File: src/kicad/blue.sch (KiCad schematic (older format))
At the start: 0 parts

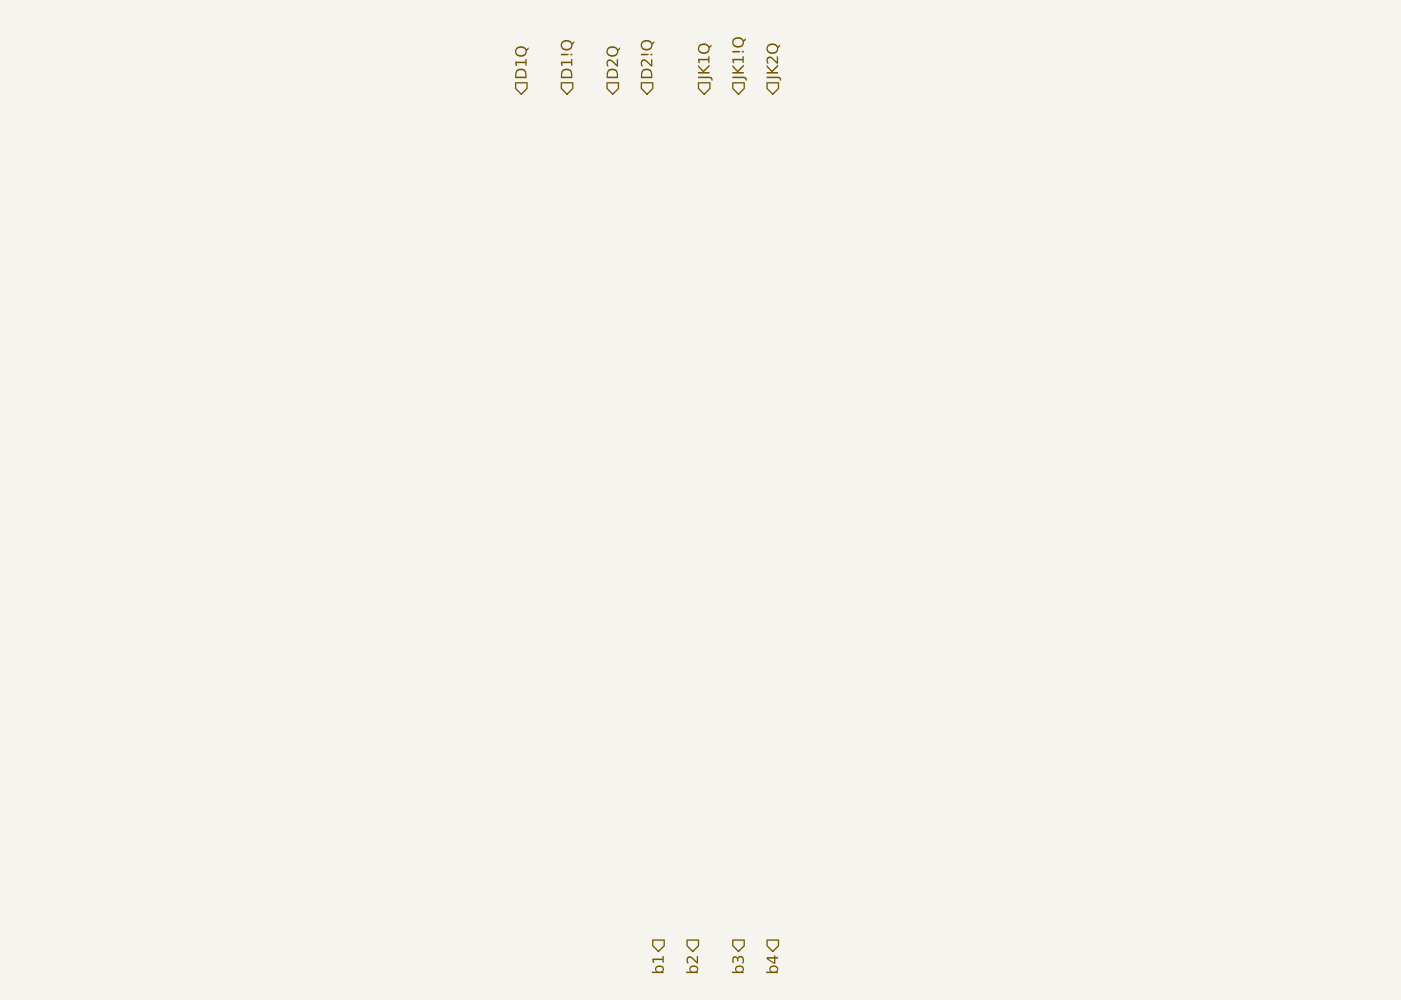
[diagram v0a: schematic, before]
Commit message: finished sub-schemes for LEDs
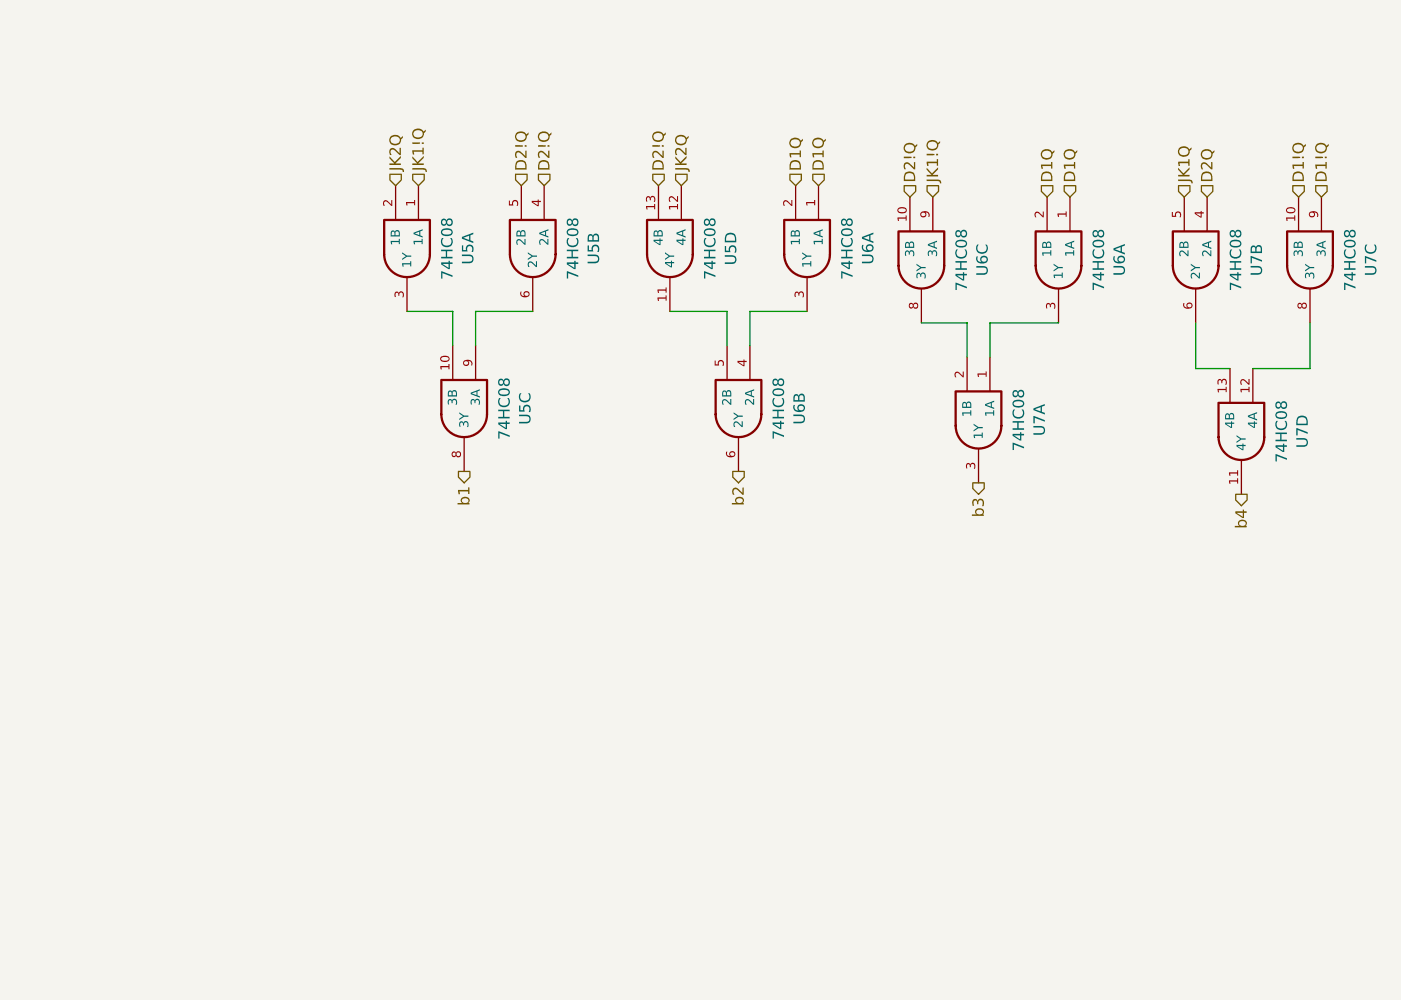
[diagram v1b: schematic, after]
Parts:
- added U5, U6 (x2), U7: 74HC08, Housings_SOIC:SOIC-14_3.9x8.7mm_Pitch1.27mm, symbol PB170:74HC08
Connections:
- net D1!Q: now also U7.10 (3B), U7.9 (3A)
- net D1Q: now also U6.1 (1A), U6.1 (1A), U6.2 (1B), U6.2 (1B)
- net D2!Q: now also U5.13 (4B), U5.4 (2A), U5.5 (2B), U6.10 (3B)
- net D2Q: now also U7.4 (2A)
- net JK1!Q: now also U5.1 (1A), U6.9 (3A)
- net JK1Q: now also U7.5 (2B)
- net JK2Q: now also U5.12 (4A), U5.2 (1B)
- net b1: now also U5.8 (3Y)
- net b2: now also U6.6 (2Y)
- net b3: now also U7.3 (1Y)
- net b4: now also U7.11 (4Y)
- new net: U5.10 (3B), U5.3 (1Y)
- new net: U5.6 (2Y), U5.9 (3A)
- new net: U5.11 (4Y), U6.5 (2B)
- new net: U6.3 (1Y), U6.4 (2A)
- new net: U6.8 (3Y), U7.2 (1B)
- new net: U6.3 (1Y), U7.1 (1A)
- new net: U7.13 (4B), U7.6 (2Y)
- new net: U7.12 (4A), U7.8 (3Y)

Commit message: fixed annotaion
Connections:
- net D1Q: now also U6.12 (4A), U6.13 (4B); no longer U6.1 (1A), U6.2 (1B)
- net at U7.1 (1A): now also U6.11 (4Y); no longer U6.3 (1Y)
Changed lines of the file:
@@
 $Descr A4 11693 8268
 encoding utf-8
-Sheet 4 6
+Sheet 3 5
 Title ""
 Date ""
@@
 $Comp
 L PB170:74HC08 U?
-U 1 1 5FFF44C7
+U 4 1 5FFF44C7
 P 5150 2700
 AR Path="/5FFF44C7" Ref="U?"  Part="2"
 AR Path="/6006FC3B/5FFF44C7" Ref="U?"  Part="4"
-AR Path="/6004480C/5FFF44C7" Ref="U6"  Part="1"
+AR Path="/6004480C/5FFF44C7" Ref="U6"  Part="4"
 F 0 "U6" H 5175 2967 50  0000 C CNN
 F 1 "74HC08" H 5175 2876 50  0000 C CNN
@@
 F 3 "https://datasheet.lcsc.com/szlcsc/Nexperia-74HC08D-653_C5593.pdf" H 5150 2700 50  0001 C CNN
 F 4 "C5593" H 5150 2700 50  0001 C CNN "LCSC"
-	1    5150 2700
+	4    5150 2700
 	0    1    1    0
 $EndComp

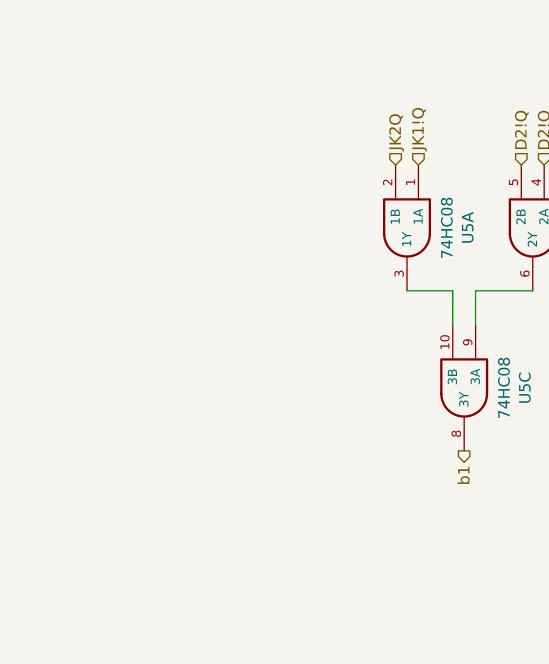
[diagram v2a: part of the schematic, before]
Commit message: added annotations, power connections to parts
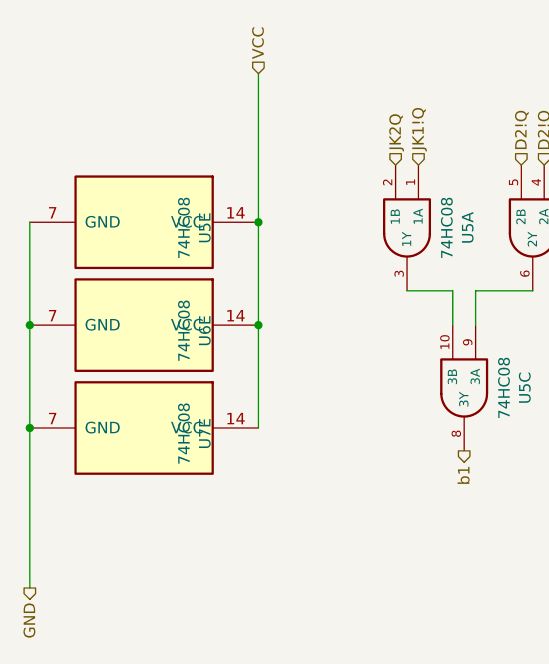
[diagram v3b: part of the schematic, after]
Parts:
- added unit 5 of U5
- added unit 5 of U6
- added unit 5 of U7
- U5, U6, U7: footprint Housings_SOIC:SOIC-14_3.9x8.7mm_Pitch1.27mm -> Package_SO:SOIC-14_3.9x8.7mm_P1.27mm
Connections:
- new net GND: U5.7 (GND), U6.7 (GND), U7.7 (GND)
- new net VCC: U5.14 (VCC), U6.14 (VCC), U7.14 (VCC)
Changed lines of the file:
@@
 F 0 "U5" H 2325 2917 50  0000 C CNN
 F 1 "74HC08" H 2325 2826 50  0000 C CNN
-F 2 "Housings_SOIC:SOIC-14_3.9x8.7mm_Pitch1.27mm" H 2300 2650 50  0001 C CNN
+F 2 "Package_SO:SOIC-14_3.9x8.7mm_P1.27mm" H 2300 2650 50  0001 C CNN
 F 3 "https://datasheet.lcsc.com/szlcsc/Nexperia-74HC08D-653_C5593.pdf" H 2300 2650 50  0001 C CNN
 F 4 "C5593" H 2300 2650 50  0001 C CNN "LCSC"
@@
 F 0 "U5" H 2875 2917 50  0000 C CNN
 F 1 "74HC08" H 2875 2826 50  0000 C CNN
-F 2 "Housings_SOIC:SOIC-14_3.9x8.7mm_Pitch1.27mm" H 2850 2650 50  0001 C CNN
+F 2 "Package_SO:SOIC-14_3.9x8.7mm_P1.27mm" H 2850 2650 50  0001 C CNN
 F 3 "https://datasheet.lcsc.com/szlcsc/Nexperia-74HC08D-653_C5593.pdf" H 2850 2650 50  0001 C CNN
 F 4 "C5593" H 2850 2650 50  0001 C CNN "LCSC"
@@
 F 0 "U5" H 2575 3617 50  0000 C CNN
 F 1 "74HC08" H 2575 3526 50  0000 C CNN
-F 2 "Housings_SOIC:SOIC-14_3.9x8.7mm_Pitch1.27mm" H 2550 3350 50  0001 C CNN
+F 2 "Package_SO:SOIC-14_3.9x8.7mm_P1.27mm" H 2550 3350 50  0001 C CNN
 F 3 "https://datasheet.lcsc.com/szlcsc/Nexperia-74HC08D-653_C5593.pdf" H 2550 3350 50  0001 C CNN
 F 4 "C5593" H 2550 3350 50  0001 C CNN "LCSC"
@@
 F 0 "U5" H 3475 2917 50  0000 C CNN
 F 1 "74HC08" H 3475 2826 50  0000 C CNN
-F 2 "Housings_SOIC:SOIC-14_3.9x8.7mm_Pitch1.27mm" H 3450 2650 50  0001 C CNN
+F 2 "Package_SO:SOIC-14_3.9x8.7mm_P1.27mm" H 3450 2650 50  0001 C CNN
 F 3 "https://datasheet.lcsc.com/szlcsc/Nexperia-74HC08D-653_C5593.pdf" H 3450 2650 50  0001 C CNN
 F 4 "C5593" H 3450 2650 50  0001 C CNN "LCSC"
@@
 F 0 "U6" H 4075 2917 50  0000 C CNN
 F 1 "74HC08" H 4075 2826 50  0000 C CNN
-F 2 "Housings_SOIC:SOIC-14_3.9x8.7mm_Pitch1.27mm" H 4050 2650 50  0001 C CNN
+F 2 "Package_SO:SOIC-14_3.9x8.7mm_P1.27mm" H 4050 2650 50  0001 C CNN
 F 3 "https://datasheet.lcsc.com/szlcsc/Nexperia-74HC08D-653_C5593.pdf" H 4050 2650 50  0001 C CNN
 F 4 "C5593" H 4050 2650 50  0001 C CNN "LCSC"
@@
 F 0 "U6" H 3775 3617 50  0000 C CNN
 F 1 "74HC08" H 3775 3526 50  0000 C CNN
-F 2 "Housings_SOIC:SOIC-14_3.9x8.7mm_Pitch1.27mm" H 3750 3350 50  0001 C CNN
+F 2 "Package_SO:SOIC-14_3.9x8.7mm_P1.27mm" H 3750 3350 50  0001 C CNN
 F 3 "https://datasheet.lcsc.com/szlcsc/Nexperia-74HC08D-653_C5593.pdf" H 3750 3350 50  0001 C CNN
 F 4 "C5593" H 3750 3350 50  0001 C CNN "LCSC"
@@
 F 0 "U6" H 4575 2967 50  0000 C CNN
 F 1 "74HC08" H 4575 2876 50  0000 C CNN
-F 2 "Housings_SOIC:SOIC-14_3.9x8.7mm_Pitch1.27mm" H 4550 2700 50  0001 C CNN
+F 2 "Package_SO:SOIC-14_3.9x8.7mm_P1.27mm" H 4550 2700 50  0001 C CNN
 F 3 "https://datasheet.lcsc.com/szlcsc/Nexperia-74HC08D-653_C5593.pdf" H 4550 2700 50  0001 C CNN
 F 4 "C5593" H 4550 2700 50  0001 C CNN "LCSC"
@@
 F 0 "U6" H 5175 2967 50  0000 C CNN
 F 1 "74HC08" H 5175 2876 50  0000 C CNN
-F 2 "Housings_SOIC:SOIC-14_3.9x8.7mm_Pitch1.27mm" H 5150 2700 50  0001 C CNN
+F 2 "Package_SO:SOIC-14_3.9x8.7mm_P1.27mm" H 5150 2700 50  0001 C CNN
 F 3 "https://datasheet.lcsc.com/szlcsc/Nexperia-74HC08D-653_C5593.pdf" H 5150 2700 50  0001 C CNN
 F 4 "C5593" H 5150 2700 50  0001 C CNN "LCSC"
@@
 F 0 "U7" H 4825 3667 50  0000 C CNN
 F 1 "74HC08" H 4825 3576 50  0000 C CNN
-F 2 "Housings_SOIC:SOIC-14_3.9x8.7mm_Pitch1.27mm" H 4800 3400 50  0001 C CNN
+F 2 "Package_SO:SOIC-14_3.9x8.7mm_P1.27mm" H 4800 3400 50  0001 C CNN
 F 3 "https://datasheet.lcsc.com/szlcsc/Nexperia-74HC08D-653_C5593.pdf" H 4800 3400 50  0001 C CNN
 F 4 "C5593" H 4800 3400 50  0001 C CNN "LCSC"
@@
 F 0 "U7" H 5775 2967 50  0000 C CNN
 F 1 "74HC08" H 5775 2876 50  0000 C CNN
-F 2 "Housings_SOIC:SOIC-14_3.9x8.7mm_Pitch1.27mm" H 5750 2700 50  0001 C CNN
+F 2 "Package_SO:SOIC-14_3.9x8.7mm_P1.27mm" H 5750 2700 50  0001 C CNN
 F 3 "https://datasheet.lcsc.com/szlcsc/Nexperia-74HC08D-653_C5593.pdf" H 5750 2700 50  0001 C CNN
 F 4 "C5593" H 5750 2700 50  0001 C CNN "LCSC"
@@
 F 0 "U7" H 6275 2967 50  0000 C CNN
 F 1 "74HC08" H 6275 2876 50  0000 C CNN
-F 2 "Housings_SOIC:SOIC-14_3.9x8.7mm_Pitch1.27mm" H 6250 2700 50  0001 C CNN
+F 2 "Package_SO:SOIC-14_3.9x8.7mm_P1.27mm" H 6250 2700 50  0001 C CNN
 F 3 "https://datasheet.lcsc.com/szlcsc/Nexperia-74HC08D-653_C5593.pdf" H 6250 2700 50  0001 C CNN
 F 4 "C5593" H 6250 2700 50  0001 C CNN "LCSC"
@@
 F 0 "U7" H 5975 3717 50  0000 C CNN
 F 1 "74HC08" H 5975 3626 50  0000 C CNN
-F 2 "Housings_SOIC:SOIC-14_3.9x8.7mm_Pitch1.27mm" H 5950 3450 50  0001 C CNN
+F 2 "Package_SO:SOIC-14_3.9x8.7mm_P1.27mm" H 5950 3450 50  0001 C CNN
 F 3 "https://datasheet.lcsc.com/szlcsc/Nexperia-74HC08D-653_C5593.pdf" H 5950 3450 50  0001 C CNN
 F 4 "C5593" H 5950 3450 50  0001 C CNN "LCSC"
@@
 Text HLabel 6300 2450 1    50   Input ~ 0
 D1!Q
+$Comp
+L PB170:74HC08 U?
+U 5 1 60660C51
+P 1150 2650
+AR Path="/60660C51" Ref="U?"  Part="2"
+AR Path="/6006FC3B/60660C51" Ref="U?"  Part="4"
+AR Path="/6004480C/60660C51" Ref="U5"  Part="5"
+F 0 "U5" H 1175 2917 50  0000 C CNN
+F 1 "74HC08" H 1175 2826 50  0000 C CNN
+F 2 "Package_SO:SOIC-14_3.9x8.7mm_P1.27mm" H 1150 2650 50  0001 C CNN
+F 3 "https://datasheet.lcsc.com/szlcsc/Nexperia-74HC08D-653_C5593.pdf" H 1150 2650 50  0001 C CNN
+F 4 "C5593" H 1150 2650 50  0001 C CNN "LCSC"
+	5    1150 2650
+	0    1    1    0
+$EndComp
+$Comp
+L PB170:74HC08 U?
+U 5 1 6066226F
+P 1150 3100
+AR Path="/6066226F" Ref="U?"  Part="2"
+AR Path="/6006FC3B/6066226F" Ref="U?"  Part="4"
+AR Path="/6004480C/6066226F" Ref="U6"  Part="5"
+F 0 "U6" H 1175 3367 50  0000 C CNN
+F 1 "74HC08" H 1175 3276 50  0000 C CNN
+F 2 "Package_SO:SOIC-14_3.9x8.7mm_P1.27mm" H 1150 3100 50  0001 C CNN
+F 3 "https://datasheet.lcsc.com/szlcsc/Nexperia-74HC08D-653_C5593.pdf" H 1150 3100 50  0001 C CNN
+F 4 "C5593" H 1150 3100 50  0001 C CNN "LCSC"
+	5    1150 3100
+	0    1    1    0
+$EndComp
+$Comp
+L PB170:74HC08 U?
+U 5 1 60662D05
+P 1150 3550
+AR Path="/60662D05" Ref="U?"  Part="2"
+AR Path="/6006FC3B/60662D05" Ref="U?"  Part="4"
+AR Path="/6004480C/60662D05" Ref="U7"  Part="5"
+F 0 "U7" H 1175 3817 50  0000 C CNN
+F 1 "74HC08" H 1175 3726 50  0000 C CNN
+F 2 "Package_SO:SOIC-14_3.9x8.7mm_P1.27mm" H 1150 3550 50  0001 C CNN
+F 3 "https://datasheet.lcsc.com/szlcsc/Nexperia-74HC08D-653_C5593.pdf" H 1150 3550 50  0001 C CNN
+F 4 "C5593" H 1150 3550 50  0001 C CNN "LCSC"
+	5    1150 3550
+	0    1    1    0
+$EndComp
+Wire Wire Line
+	1650 3550 1650 3100
+Wire Wire Line
+	1650 2650 1650 3100
+Connection ~ 1650 3100
+Wire Wire Line
+	1650 2650 1650 2000
+Connection ~ 1650 2650
+Wire Wire Line
+	650  2650 650  3100
+Wire Wire Line
+	650  3100 650  3550
+Connection ~ 650  3100
+Wire Wire Line
+	650  3550 650  4250
+Connection ~ 650  3550
+Text HLabel 1650 2000 1    50   Input ~ 0
+VCC
+Text HLabel 650  4250 3    50   Output ~ 0
+GND
 $EndSCHEMATC

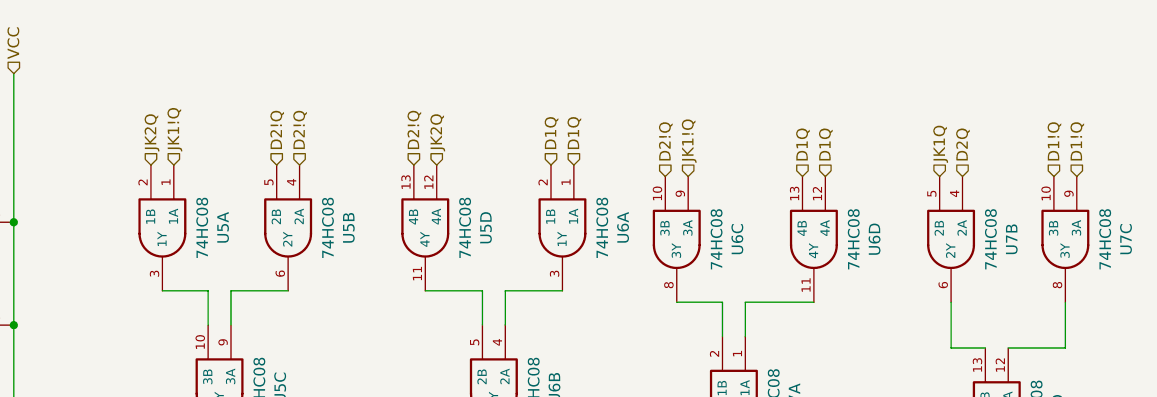
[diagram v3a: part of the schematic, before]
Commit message: Corrected negations
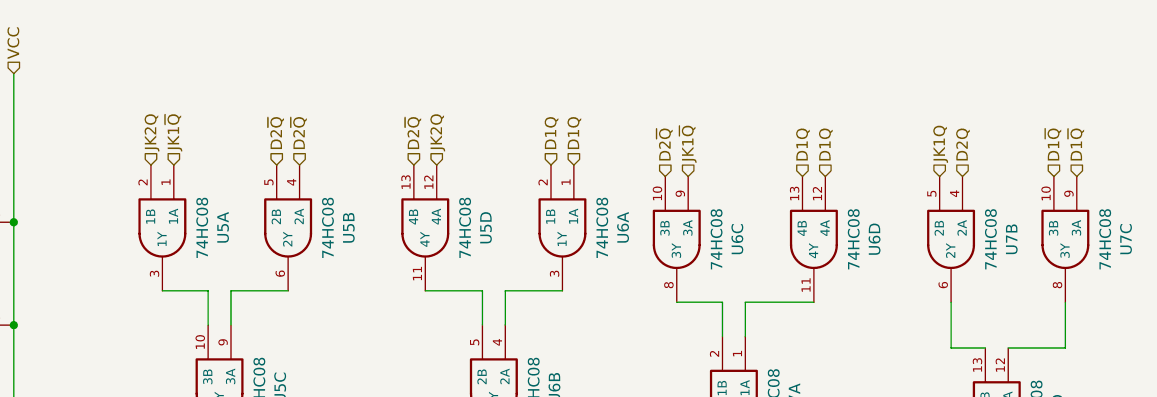
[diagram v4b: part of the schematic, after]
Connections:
- net D1!Q renamed D1~Q
- net D2!Q renamed D2~Q
- net JK1!Q renamed JK1~Q
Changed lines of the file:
@@
 D1Q
 Text HLabel 6200 2450 1    50   Input ~ 0
-D1!Q
+D1~Q
 Text HLabel 5800 2450 1    50   Input ~ 0
 D2Q
 Text HLabel 2800 2400 1    50   Input ~ 0
-D2!Q
+D2~Q
 Text HLabel 5700 2450 1    50   Input ~ 0
 JK1Q
 Text HLabel 2350 2400 1    50   Input ~ 0
-JK1!Q
+JK1~Q
 Text HLabel 2250 2400 1    50   Input ~ 0
 JK2Q
@@
 	2600 2950 2850 2950
 Text HLabel 2900 2400 1    50   Input ~ 0
-D2!Q
+D2~Q
 $Comp
 L PB170:74HC08 U?
@@
 	3700 2950 3700 3100
 Text HLabel 3400 2400 1    50   Input ~ 0
-D2!Q
+D2~Q
 Text HLabel 3500 2400 1    50   Input ~ 0
 JK2Q
@@
 	4850 3000 4850 3150
 Text HLabel 4600 2450 1    50   Input ~ 0
-JK1!Q
+JK1~Q
 Text HLabel 4500 2450 1    50   Input ~ 0
-D2!Q
+D2~Q
 Text HLabel 5100 2450 1    50   Input ~ 0
 D1Q
@@
 	6250 3200 6000 3200
 Text HLabel 6300 2450 1    50   Input ~ 0
-D1!Q
-$Comp
-L PB170:74HC08 U?
+D1~Q
+$Comp
+L PB170:74HC08 U?
